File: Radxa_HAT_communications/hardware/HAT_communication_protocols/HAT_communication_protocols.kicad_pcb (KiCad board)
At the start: 2 copper layers, 63.2 x 35 mm, 57 parts, among them J1 Conn_01x02_Pin, J2 Can_terminals, J3 120Can-resistor, J4 Power_supply_12V, J5 LoRa_DIO, Q1 NMOS, U1 AMS1117-5.0, U2 LD1117V33, U3 74HC04, U4 MAX3485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

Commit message: new docummentation
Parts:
- removed C15: 100nf, Resistor_SMD:R_0603_1608Metric_Pad0.98x0.95mm_HandSolder
- added 2-Pin_Power_input1: Conn_01x02, Connector_PinHeader_2.54mm:PinHeader_1x02_P2.54mm_Vertical, F.Cu at (129.6, 114.7)
- added C17: 10uf, Resistor_SMD:R_0603_1608Metric_Pad0.98x0.95mm_HandSolder, F.Cu at (89.0, 92.4)
- added C18: 1uf, Resistor_SMD:R_0603_1608Metric_Pad0.98x0.95mm_HandSolder, F.Cu at (86.5, 92.4)
- added C19: 10uf, Resistor_SMD:R_0603_1608Metric_Pad0.98x0.95mm_HandSolder, F.Cu at (101.6, 96.8)
- added R4: 56k, Resistor_SMD:R_0603_1608Metric_Pad0.98x0.95mm_HandSolder, F.Cu at (91.5, 96.8)
- added R9: 120, Resistor_SMD:R_0603_1608Metric_Pad0.98x0.95mm_HandSolder, F.Cu at (96.5, 101.1)
- added U7: LD1117V33, Package_TO_SOT_SMD:SOT-223-3_TabPin2, F.Cu at (63.9, 72.7)
- R2, R3: value 1K8 -> 2k4
- Y1: value 10MHz -> 8MHz
- moved RadxaGPIO1 140.4 mm to (173.1, 69.7), turned to -90 degrees
- moved H3 133.0 mm to (178.0, 120.0)
- moved H4 116.4 mm to (178.0, 71.0), turned to 180 degrees
- moved Q1 102.5 mm to (79.7, 132.0), turned to -90 degrees
- moved D1 94.3 mm to (94.4, 116.5), turned to -90 degrees
- moved H2 92.1 mm to (120.0, 120.0)
- moved uart_RX1 90.8 mm to (91.0, 116.5), turned to -90 degrees
- moved J4 87.5 mm to (138.7, 120.0), turned to 180 degrees
- moved uart_TX1 87.5 mm to (87.6, 116.5), turned to -90 degrees
- moved F1 84.9 mm to (73.2, 115.4), turned to -90 degrees
- moved F2 75.5 mm to (82.2, 116.1), turned to -90 degrees
- moved D4 75.5 mm to (51.5, 99.8), turned to -90 degrees
- moved D5 72.9 mm to (64.1, 92.9), turned to -90 degrees
- moved C4 72.2 mm to (101.6, 88.1), turned to -90 degrees
- moved R7 72.0 mm to (101.6, 101.1), turned to -90 degrees
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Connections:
- C16 pad 1: PS+3.3v -> LoRa+3.3v
- C4 pad 1: 12V -> Net-(U2-VI)
- C5 pad 1: 12V -> Net-(U1-VI)
- F2 pad 2: Net-(J1-Pin_1) -> Net-(RS485_interface1-Pin_1)
- J1 pad 1: Net-(J1-Pin_1) -> Net-(D5-A1)
- R10 pad 1: Net-(J2-Pin_1) -> Net-(J2-Pin_2)
- R5 pad 2: /TXD -> /GPIO20
- RS485_interface1 pad 1: Net-(J1-Pin_1) -> Net-(RS485_interface1-Pin_1)
- RadxaGPIO1 pad 11: /GPIO05 -> /CAN_CS
- RadxaGPIO1 pad 13: /GPIO06 -> /CAN_SCK
- RadxaGPIO1 pad 15: /GPIO03 -> /CAN_SI
- RadxaGPIO1 pad 6: /GPIO20 -> GND
- RadxaGPIO1 pad 7: /GPIO04 -> /CAN_SO
- RadxaGPIO1 pad 8: GND -> /GPIO20
- SX1 pad 13: PS+3.3v -> LoRa+3.3v
- SX1 pad 2: /LoRa_SO -> /CAN_SO
- SX1 pad 3: /LoRa_SI -> /CAN_SI
- SX1 pad 4: /LoRa_SCK -> /CAN_SCK
- SX1 pad 5: /LoRa_NSS -> /CAN_CS
- U1 pad 3: 12V -> Net-(U1-VI)
- U2 pad 3: 12V -> Net-(U2-VI)
- U3 pad 1: /TXD -> /GPIO20
- U3 pad 4: /RXD -> /GPIO21
- U3 pad 5: /RXD -> /GPIO21
- U6 pad 5: PS+5v -> unconnected-(U6-VIO-Pad5)
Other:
- board size 63.2 x 35 mm -> 65 x 56 mm

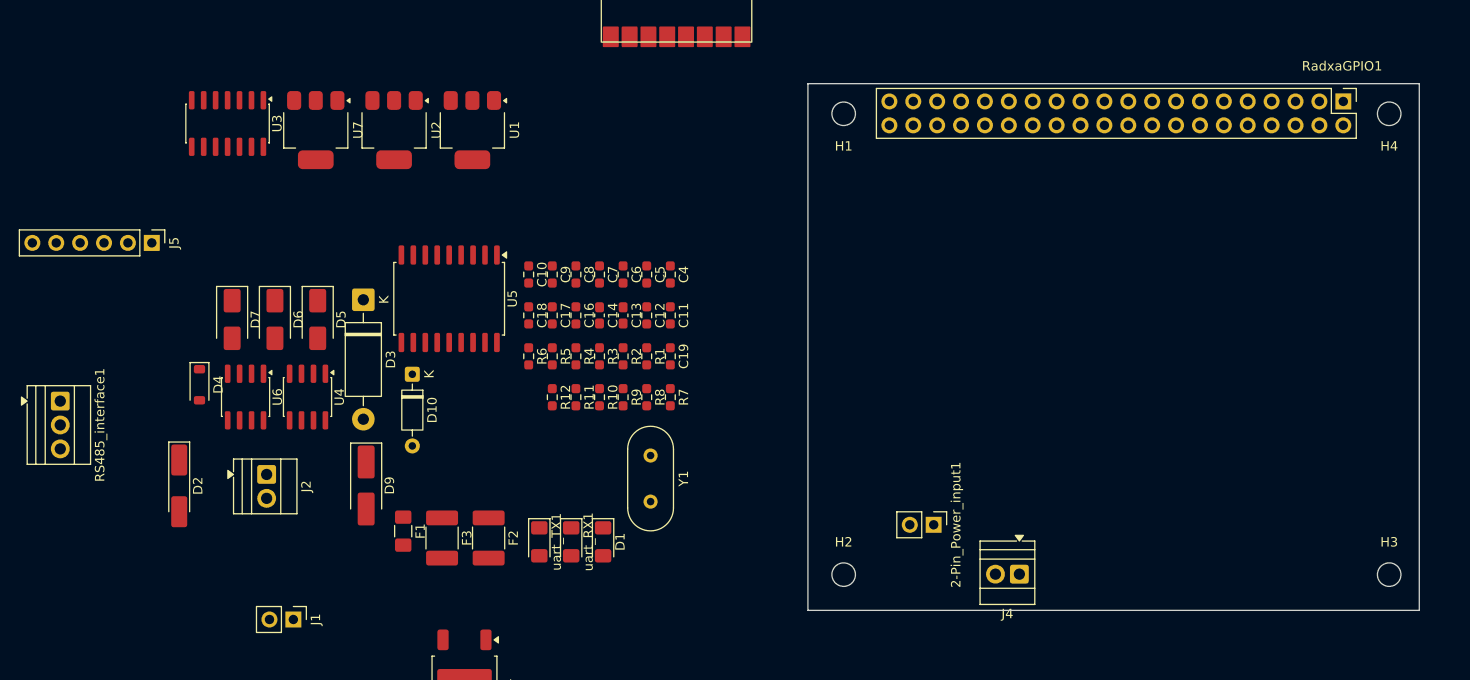
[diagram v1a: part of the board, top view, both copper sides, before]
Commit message: PCB design | PCB countors finally drew and correct placement of pinheaders and pin socker so they fit to the Radxa-X4 form factor
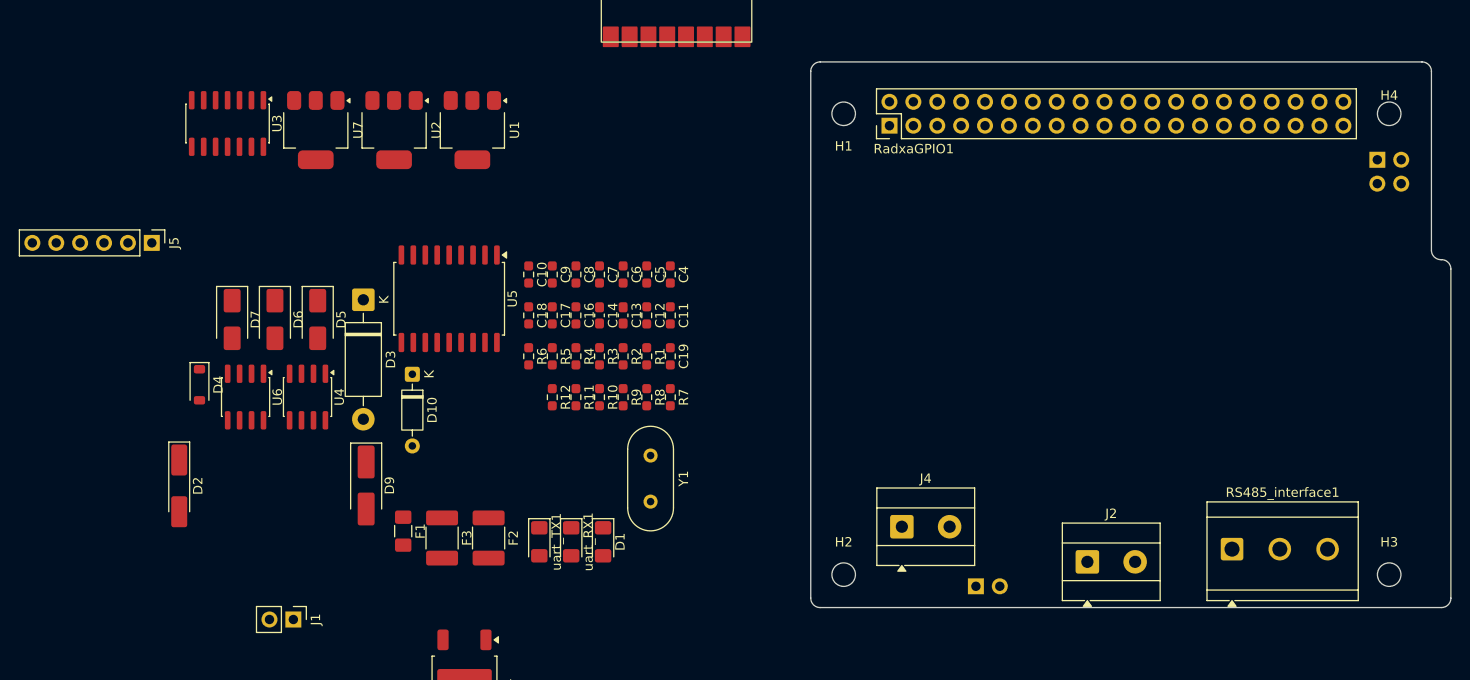
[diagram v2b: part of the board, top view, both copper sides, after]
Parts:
- added J6: PoE, Connector_PinSocket_2.54mm:PinSocket_2x02_P2.54mm_Vertical, B.Cu at (176.7, 75.9)
- 2-Pin_Power_input1: footprint Connector_PinHeader_2.54mm:PinHeader_1x02_P2.54mm_Vertical -> Connector_PinSocket_2.54mm:PinSocket_1x02_P2.54mm_Vertical; moved to B.Cu
- J2, J4: footprint TerminalBlock:TerminalBlock_Xinya_XY308-2.54-2P_1x02_P2.54mm_Horizontal -> TerminalBlock_MetzConnect:TerminalBlock_MetzConnect_Type101_RT01602HBWC_1x02_P5.08mm_Horizontal
- RS485_interface1: footprint TerminalBlock:TerminalBlock_Xinya_XY308-2.54-3P_1x03_P2.54mm_Horizontal -> TerminalBlock_CUI:TerminalBlock_CUI_TB007-508-03_1x03_P5.08mm_Horizontal
- moved RS485_interface1 125.6 mm to (161.3, 117.3), turned to 0 degrees
- moved J2 87.8 mm to (145.9, 118.6), turned to 0 degrees
- moved RadxaGPIO1 48.3 mm to (124.9, 72.3), turned to 90 degrees
- moved J4 13.5 mm to (126.2, 114.9), turned to 0 degrees
- moved 2-Pin_Power_input1 7.93 mm to (134.1, 121.2)
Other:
- board size 65 x 56 mm -> 68.1 x 58 mm

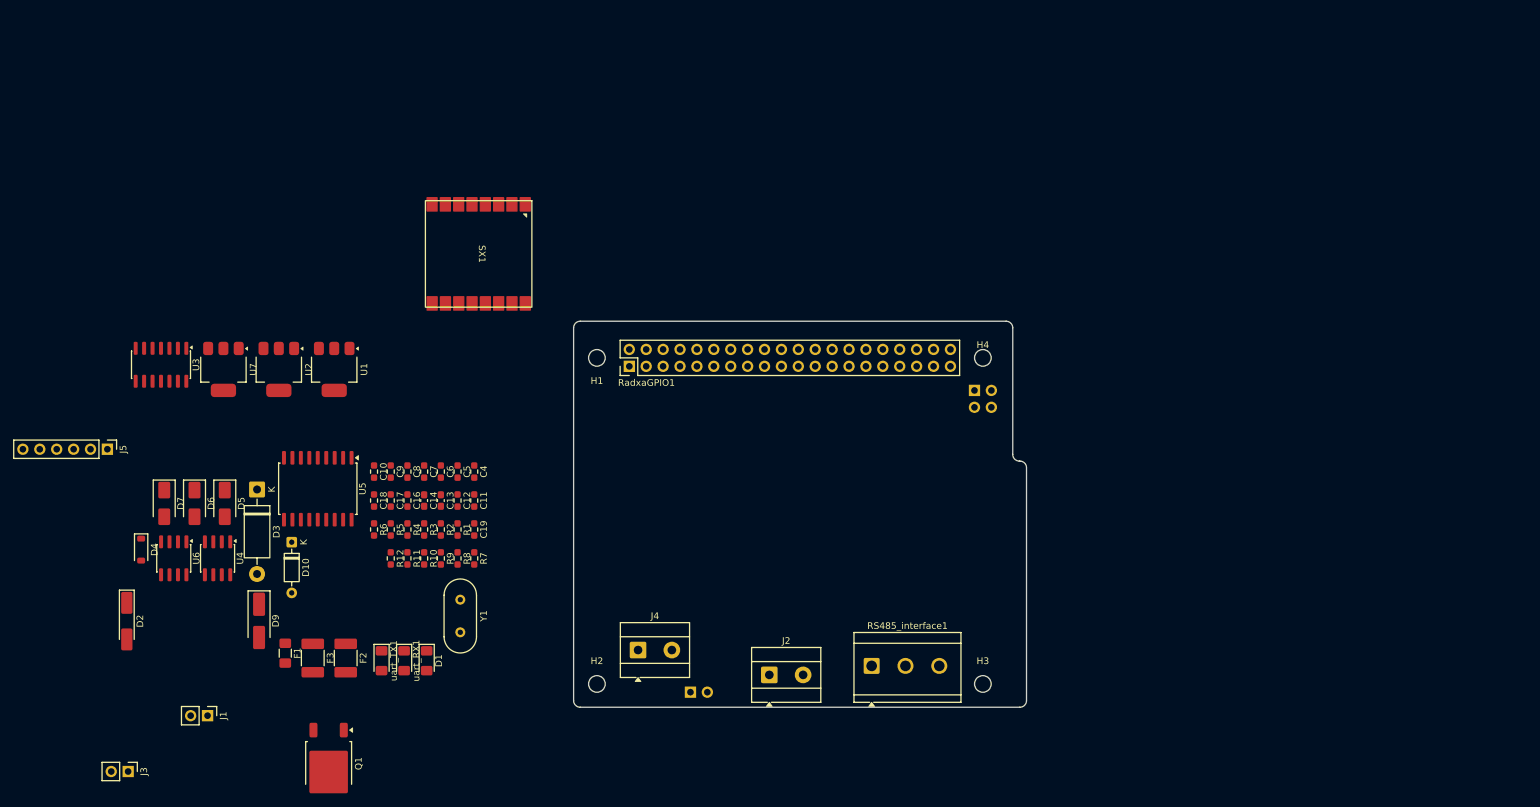
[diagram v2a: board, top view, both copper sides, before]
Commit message: Placement of some components in PCB layout. Thinking on adding a buck converter
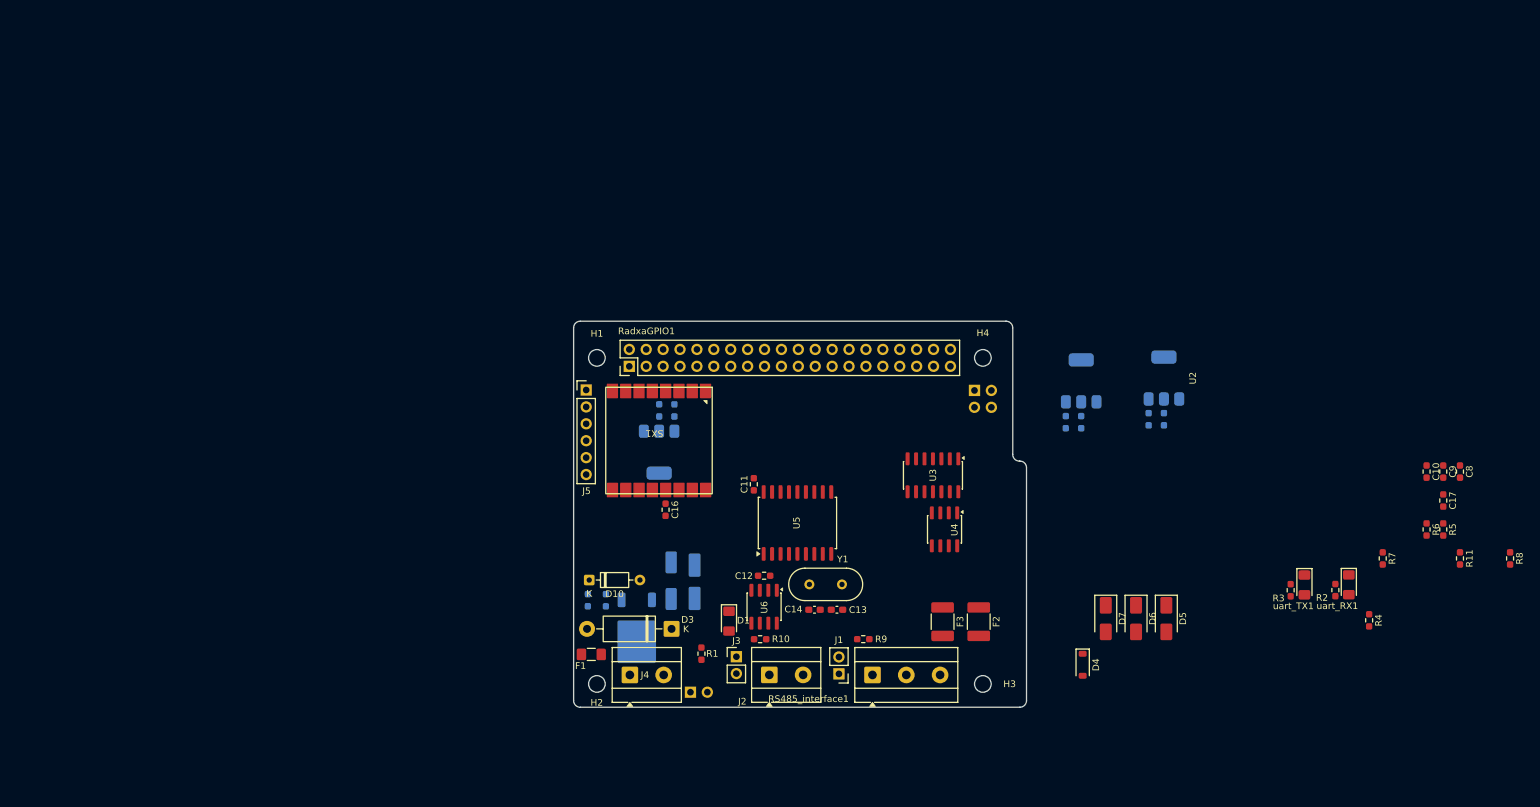
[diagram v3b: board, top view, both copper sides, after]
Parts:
- added R13: 10, Resistor_SMD:R_0603_1608Metric_Pad0.98x0.95mm_HandSolder, B.Cu at (121.3, 107.4)
- C18, C19, C4, C5, C6, C7, D2, D9, Q1, R12, U1, U2, U7: moved to B.Cu
- J4: value Power_supply_12V -> PS-12V
- RS485_interface1: footprint TerminalBlock_CUI:TerminalBlock_CUI_TB007-508-03_1x03_P5.08mm_Horizontal -> TerminalBlock_MetzConnect:TerminalBlock_MetzConnect_Type101_RT01603HBWC_1x03_P5.08mm_Horizontal
- moved C10 158.2 mm to (244.7, 88.1)
- moved C17 158.2 mm to (247.2, 92.4)
- moved C9 158.2 mm to (247.2, 88.1)
- moved R5 158.2 mm to (247.2, 96.8)
- moved R6 158.2 mm to (244.7, 96.8)
- moved R8 158.2 mm to (257.2, 101.1)
- moved C8 158.2 mm to (249.7, 88.1)
- moved R11 158.2 mm to (249.7, 101.1)
- moved R4 145.2 mm to (236.1, 110.4)
- moved D4 142.5 mm to (193.0, 117.1)
- moved D5 142.5 mm to (205.6, 110.2)
- moved D6 142.5 mm to (201.0, 110.2)
- moved D7 142.5 mm to (196.5, 110.2)
- moved uart_RX1 142.4 mm to (233.0, 105.1)
- moved uart_TX1 139.2 mm to (226.3, 105.1)
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- renumbered 2-Pin_Power_input1 to IN-12V1
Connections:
- F1 pad 1: Net-(J4-Pin_2) -> Net-(J4-Pin_1)
- J4 pad 1: Net-(D3-A1) -> Net-(J4-Pin_1)
- J4 pad 2: Net-(J4-Pin_2) -> Net-(D3-A1)
- Q1 pad 1: Net-(D10-A) -> Net-(Q1-G)

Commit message: PCB layout first version done
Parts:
- removed D10: 1N4148, Diode_THT:D_DO-35_SOD27_P7.62mm_Horizontal
- added AE1: Antenna, Connector_PinHeader_2.54mm:PinHeader_1x01_P2.54mm_Vertical, F.Cu at (118.5, 75.7)
- added C1: 10uF /25v, Capacitor_SMD:C_1206_3216Metric_Pad1.33x1.80mm_HandSolder, F.Cu at (118.5, 101.1)
- added C15: 10nf, Resistor_SMD:R_0603_1608Metric_Pad0.98x0.95mm_HandSolder, F.Cu at (119.7, 96.5)
- added C3: 22uF 6.3v, Capacitor_SMD:C_1206_3216Metric_Pad1.33x1.80mm_HandSolder, F.Cu at (126.1, 111.8)
- added D8: 1N4148W, Diode_SMD:D_SOD-123, B.Cu at (134.2, 98.4)
- added L2: 100uH_1.0A, Inductor_SMD:L_Wuerth_WE-PD-Typ-M-Typ-S_Handsoldering, F.Cu at (120.7, 110.8)
- added R14: 100K, Resistor_SMD:R_0603_1608Metric_Pad0.98x0.95mm_HandSolder, F.Cu at (128.5, 98.2)
- added R15: 6k8, Resistor_SMD:R_0603_1608Metric_Pad0.98x0.95mm_HandSolder, F.Cu at (128.4, 105.1)
- added R16: 10k, Resistor_SMD:R_0603_1608Metric_Pad0.98x0.95mm_HandSolder, F.Cu at (126.5, 104.8)
- added R17: 10k, Resistor_SMD:R_0603_1608Metric_Pad0.98x0.95mm_HandSolder, F.Cu at (124.6, 104.8)
- C10, C11, C12, C16, C17, C8, C9, D4, F2, F3, R10, R11, R2, R3, R4, R5, R6, R7, R8, R9: moved to B.Cu
- C18, C19, C5, C6, U1, U7: moved to F.Cu
- C4: value 10uf -> 100nf; moved to F.Cu
- C7: value 1uf -> 3.9nf; moved to F.Cu
- U2: value LD1117V33 -> MP2307; footprint Package_TO_SOT_SMD:SOT-223-3_TabPin2 -> Package_SO:SOIC-8-1EP_3.9x4.9mm_P1.27mm_EP2.62x3.51mm; moved to F.Cu
- moved C17 100.8 mm to (146.4, 89.5)
- moved R11 100.7 mm to (149.6, 89.5), turned to 90 degrees
- moved C9 90.0 mm to (157.2, 91.6), turned to 90 degrees
- moved R8 90.0 mm to (167.3, 100.6), turned to 90 degrees
- moved U2 85.6 mm to (123.7, 100.2), turned to 0 degrees
- moved C10 79.9 mm to (165.7, 100.6), turned to 90 degrees
- moved C7 79.7 mm to (128.4, 101.6)
- moved R4 79.5 mm to (158.8, 91.5)
- moved C8 77.9 mm to (171.9, 91.9), turned to 0 degrees
- moved C4 77.7 mm to (126.8, 95.9), turned to 90 degrees
- moved R5 75.8 mm to (172.0, 87.4), turned to 180 degrees
- moved R6 74.7 mm to (170.0, 95.8), turned to 180 degrees
- moved R7 69.3 mm to (168.8, 100.6), turned to 90 degrees
- moved U1 61.6 mm to (135.1, 96.0), turned to 180 degrees
- moved uart_RX1 61.0 mm to (172.0, 103.1)
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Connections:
- C16 pad 1: LoRa+3.3v -> PS+3.3v
- C18 pad 1: LoRa+3.3v -> PS+3.3v
- C19 pad 1: Net-(U7-VI) -> PS+5v
- C4 pad 1: Net-(U2-VI) -> Net-(U2-SS)
- C5 pad 1: Net-(U1-VI) -> PS+6.2v
- C7 pad 1: PS+3.3v -> Net-(U2-COMP)
- C7 pad 2: GND -> Net-(C7-Pad2)
- D3 pad 2: Net-(D10-K) -> 12V
- D9 pad 1: Net-(D10-K) -> 12V
- F1 pad 2: Net-(D10-K) -> 12V
- F2 pad 2: Net-(RS485_interface1-Pin_1) -> Net-(RS485_interface1-Pin_3)
- J3 pad 2: Net-(J2-Pin_1) -> Net-(J2-Pin_2)
- R1 pad 1: 12V -> PS+6.2v
- R10 pad 1: Net-(J2-Pin_2) -> Net-(J2-Pin_1)
- R12 pad 2: Net-(D10-K) -> 12V
- RS485_interface1 pad 1: Net-(RS485_interface1-Pin_1) -> /COMs
- RS485_interface1 pad 3: /COMs -> Net-(RS485_interface1-Pin_3)
- SX1 pad 13: LoRa+3.3v -> PS+3.3v
- U1 pad 3: Net-(U1-VI) -> PS+6.2v
- U2 pad 1: GND -> Net-(U2-BS)
- U2 pad 2: PS+3.3v -> 12V
- U2 pad 3: Net-(U2-VI) -> Net-(U2-SW)
- U6 pad 6: Net-(J2-Pin_2) -> Net-(J2-Pin_1)
- U6 pad 7: Net-(J2-Pin_1) -> Net-(J2-Pin_2)
- U7 pad 2: LoRa+3.3v -> PS+3.3v
- U7 pad 3: Net-(U7-VI) -> PS+5v

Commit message: PCB tracks 60% completed
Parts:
- moved D4 7.81 mm to (167.9, 87.5)
- moved R4 7.81 mm to (165.9, 88.2)
- moved C9 7.81 mm to (164.3, 88.3)
- moved R1 7.63 mm to (125.2, 116.8), turned to -90 degrees
- moved C17 6.02 mm to (151.4, 86.1), turned to 90 degrees
- moved D1 5.79 mm to (127.2, 117.6), turned to 90 degrees
- moved C10 4.43 mm to (170.2, 100.5), turned to -90 degrees
- moved J1 4.33 mm to (172.8, 112.1)
- moved F2 4.22 mm to (168.9, 110.7)
- moved F3 4.22 mm to (164.8, 110.8)
- moved R9 4.22 mm to (168.6, 106.7)
- moved U6 4.20 mm to (150.2, 109.9)
- moved C12 3.92 mm to (150.3, 107.1)
- moved R2 3.62 mm to (175.9, 102.8)
- moved uart_RX1 3.62 mm to (175.5, 101.9)
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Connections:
- J5 pad 2: /LoRa_D1 -> /LoRa_D2
- J5 pad 3: /LoRa_D2 -> /LoRa_D1
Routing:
- net 12V: track 0.00 -> 85.1 mm, vias 0 -> 2
- net PS+6.2v: track 0.00 -> 62.8 mm
- net PS+5v: track 0.00 -> 56.6 mm, vias 0 -> 2
- net PS+3.3v: track 0.00 -> 50.2 mm, vias 0 -> 4
- net GND: track 0.00 -> 22.0 mm, vias 0 -> 12
- net /COMs: track 0.00 -> 19.3 mm
- net /LoRa_D5: track 0.00 -> 19.2 mm, vias 0 -> 1
- net Net-(D5-A1): track 0.00 -> 15.4 mm, vias 0 -> 1
- net Net-(J2-Pin_2): track 0.00 -> 15.3 mm
- net Net-(U2-SW): track 0.00 -> 14.5 mm
- net /RCcan-RXD: track 0.00 -> 14.3 mm
- net /LoRa_D0: track 0.00 -> 13.6 mm
- net Net-(D6-A1): track 0.00 -> 13.6 mm, vias 0 -> 1
- net Net-(D3-A1): track 0.00 -> 13.2 mm
- net /TXcan-TXD: track 0.00 -> 10.4 mm
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
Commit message: PCB V1 done
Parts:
- R2, R3: moved to F.Cu
- moved C9 8.51 mm to (156.6, 91.8)
- moved D4 8.50 mm to (160.2, 91.2)
- moved R4 8.49 mm to (158.2, 91.8)
- moved uart_TX1 8.07 mm to (173.6, 96.1)
- moved uart_RX1 7.28 mm to (171.2, 96.1)
- moved R3 7.07 mm to (175.6, 96.9)
- moved R5 6.74 mm to (173.3, 91.9), turned to 90 degrees
- moved R2 6.02 mm to (177.2, 96.9)
- moved R6 5.59 mm to (172.0, 100.1), turned to 90 degrees
- moved C10 3.38 mm to (173.5, 100.0), turned to 90 degrees
- moved R7 3.23 mm to (170.4, 100.1), turned to 90 degrees
- moved R8 3.01 mm to (171.2, 102.5)
- moved U3 2.24 mm to (166.1, 89.9)
- moved C8 1.86 mm to (171.7, 91.8), turned to 90 degrees
- moved C16 1.51 mm to (124.7, 84.7), turned to -90 degrees
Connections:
- RadxaGPIO1 pad 1: 3.3v_gpio -> 3.3v_pin1
- RadxaGPIO1 pad 17: 3.3v_gpio -> 3.3v_pin17
- RadxaGPIO1 pad 2: 5v_gpio -> 5v_pin2
- RadxaGPIO1 pad 4: 5v_gpio -> 5v_pin4
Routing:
- net /GPIO20: track 0.00 -> 66.0 mm, vias 0 -> 1
- net /GPIO21: track 0.00 -> 52.3 mm
- net PS+3.3v: track 50.2 -> 100.5 mm
- net /CAN_SI: track 0.00 -> 44.8 mm
- net /CAN_CS: track 0.00 -> 41.6 mm
- net /CAN_SCK: track 0.00 -> 40.1 mm
- net /CAN_SO: track 0.00 -> 34.6 mm
- net Net-(R2-Pad1): track 0.00 -> 27.1 mm, vias 0 -> 2
- net GND: track 22.0 -> 41.5 mm, vias 12 -> 18
- net Net-(R3-Pad1): track 0.00 -> 19.0 mm
- net Net-(D4-A): track 0.00 -> 14.7 mm, vias 0 -> 1
- net Net-(D4-K): track 0.00 -> 13.6 mm, vias 0 -> 1
- net Net-(U4-RO): track 2.49 -> 14.9 mm
- net Net-(U3-Pad3): track 0.00 -> 8.31 mm
- net Net-(uart_RX1-A): track 0.00 -> 7.59 mm
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- added copper zone on B.Cu, net GND
- added copper zone on F.Cu, net GND
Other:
- board text added: "C4"

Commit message: PCB V1.2 done
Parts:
- C12, F2, F3, R9: moved to F.Cu
- R2, R3: moved to B.Cu
- moved uart_TX1 17.3 mm to (166.7, 80.2), turned to 0 degrees
- moved R3 16.8 mm to (167.4, 82.2), turned to 0 degrees
- moved R2 14.4 mm to (167.4, 86.3), turned to 0 degrees
- moved uart_RX1 12.7 mm to (166.6, 84.2), turned to 0 degrees
- moved F2 11.3 mm to (180.2, 110.7)
- moved F3 11.2 mm to (176.0, 110.7)
- moved J1 9.74 mm to (180.0, 105.5)
- moved R9 8.56 mm to (177.1, 105.8), turned to 90 degrees
- moved R7 7.88 mm to (178.2, 101.2)
- moved D6 6.77 mm to (172.0, 110.4)
- moved U4 6.47 mm to (173.1, 99.3)
- moved R6 5.97 mm to (176.7, 96.4), turned to -90 degrees
- moved D2 5.36 mm to (142.0, 101.8), turned to 0 degrees
- moved U3 5.23 mm to (171.2, 91.1)
- moved C8 5.10 mm to (176.7, 93.0)
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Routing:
- net 12V: track 85.1 -> 57.8 mm
- net Net-(R2-Pad1): track 27.1 -> 3.79 mm, vias 2 -> 1
- net Net-(D5-A1): track 18.9 -> 28.0 mm
- net /CAN_CS: track 41.6 -> 50.1 mm
- net PS+3.3v: track 100.5 -> 108.4 mm, vias 4 -> 5
- net /GPIO21: track 52.3 -> 59.7 mm
- net GND: track 41.5 -> 34.6 mm, vias 18 -> 22
- net /CAN_SCK: track 40.1 -> 46.8 mm
- net /CAN_SI: track 44.8 -> 50.5 mm
- net Net-(uart_RX1-A): track 7.59 -> 2.08 mm, vias 0 -> 1
- net /CAN_SO: track 34.6 -> 39.9 mm
- net Net-(RS485_interface1-Pin_2): track 6.70 -> 11.0 mm
- net /GPIO20: track 66.0 -> 70.0 mm
- net Net-(D6-A1): track 16.5 -> 20.2 mm, vias 2 -> 1
- net PS+6.2v: track 65.5 -> 69.2 mm
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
